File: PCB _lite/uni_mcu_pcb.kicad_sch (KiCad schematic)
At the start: 65 parts, among them J1 USB_C_Receptacle_USB2.0, J2 Conn_01x02_Male, J3 Conn_02x08_Odd_Even, Q1 Q_NPN_BCE, Q2 Q_NPN_BCE, Q3 Q_NPN_BCE, Q4 Q_NPN_BCE, Q5 FDS6890A, Q6 FDS6890A, SW1 SW_DIP_x01, SW2 SW_DIP_x01, SW3 SW_DIP_x01, U1 CC56-12CGKWA, U2 CH330N, U3 USBLC6-2P6, U4 STM32F030K6Tx, U5 LD1117S33TR_SOT223, U6 STM32F030C8Tx, U7 W25Q32JVSS, Y1 Crystal

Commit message: Добавлена lite версия платы
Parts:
- removed RN2: R_Pack05, Resistor_SMD:R_Array_Convex_5x0603, symbol Device:R_Pack05
- removed SW3: SW_DIP_x01, Button_Switch_SMD:SW_Push_1P1T_NO_Vertical_Wuerth_434133025816, symbol Switch:SW_DIP_x01
- removed U6: STM32F030C8Tx, Package_QFP:LQFP-48_7x7mm_P0.5mm, symbol MCU_ST_STM32F0:STM32F030C8Tx
- added J4: Conn_01x05_Female, TerminalBlock_MetzConnect:TerminalBlock_MetzConnect_Type011_RT05505HBWC_1x05_P5.00mm_Horizontal, symbol Connector:Conn_01x05_Female
- added R27, R28: R, Resistor_SMD:R_0603_1608Metric_Pad0.98x0.95mm_HandSolder, symbol Device:R
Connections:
- net I2C1_SDA is gone; now on net d_I2C1_SCL: R26.1
- net OUT3_CTRL is gone; now on net CA3_CTRL: R20.1, R24.2
- net OUT4_CTRL is gone; now on net CA4_CTRL: R18.1, R22.2
- net d is gone; now on net d_I2C1_SCL: U1.2 (d), U4.19 (PA9)
- net e is gone; now on net e_I2C1_SDA: U1.1 (e), U4.20 (PA10)
- net +3V3: no longer R25.2, R26.2
- net OUT1: now also J4.2 (Pin_2)
- net OUT2: now also J4.3 (Pin_3)
- net OUT3: now also J3.10 (Pin_10), J4.4 (Pin_4)
- net OUT4: now also J3.8 (Pin_8), J4.5 (Pin_5)
- net USART1_RX: no longer JP2.1 (A)
- net USART1_TX: no longer JP1.1 (A)
- net VCC: now also J4.1 (Pin_1)
- net a: now also JP1.1 (A)
- net b: now also JP2.1 (A)
- net c: now also R28.1
- net at J3.2 (Pin_2): now also R26.2
- net at J3.4 (Pin_4): now also R27.2
- net at J3.6 (Pin_6): now also R28.2
- net I2C1_SCL renamed d_I2C1_SCL
- net SW2 renamed e_I2C1_SDA
- net e_I2C1_SDA: now also R27.1
- no-connect marks 4 -> 1
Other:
- moved on the sheet: C6, C7, J3, R13, RN1, SW1, U4, Y1

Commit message: Частично разведена плата
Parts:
- removed RN1: R_Pack05, Resistor_SMD:R_Array_Convex_5x0603, symbol Device:R_Pack05
- removed U3: USBLC6-2P6, Package_TO_SOT_SMD:SOT-666, symbol Power_Protection:USBLC6-2P6
- removed U7: W25Q32JVSS, Package_SO:SOIC-8_5.23x5.23mm_P1.27mm, symbol Memory_Flash:W25Q32JVSS
- added J5: Conn_01x04_Female, Connector_Hirose:Hirose_DF11-4DP-2DSA_2x02_P2.00mm_Vertical, symbol Connector:Conn_01x04_Female
- added R29, R30, R31, R32: R, Resistor_SMD:R_0603_1608Metric_Pad0.98x0.95mm_HandSolder, symbol Device:R
- J2: footprint Connector_PinHeader_2.54mm:PinHeader_1x02_P2.54mm_Vertical -> TerminalBlock_MetzConnect:TerminalBlock_MetzConnect_Type011_RT05502HBWC_1x02_P5.00mm_Horizontal
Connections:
- net +3V3: now also J5.4 (Pin_4); no longer R15.1
- net GND: now also J5.1 (Pin_1)
- net PB0_IO: now also R15.2
- net PB1_IO: now also R29.2
- net SPI1_MISO: now also R31.2
- net SPI1_MOSI: now also R32.2
- net SPI1_SCK: now also R30.2
- net b: now also U4.22 (PA12); no longer JP2.1 (A), U4.13 (PA7)
- net c: now also JP2.1 (A), U4.13 (PA7); no longer U4.18 (PA8)
- net d_I2C1_SCL: no longer U1.2 (d), U4.19 (PA9)
- net dpx_swdio: now also J5.2 (Pin_2)
- net e_I2C1_SDA: no longer U1.1 (e), U4.20 (PA10)
- net g: now also U4.12 (PA6); no longer U4.22 (PA12)
- net swclk: now also J5.3 (Pin_3)
- net at J3.9 (Pin_9): now also R32.1
- net at J3.7 (Pin_7): now also R31.1
- net at J3.5 (Pin_5): now also R30.1
- net at J3.3 (Pin_3): now also R29.1
- net at J3.1 (Pin_1): now also R15.1
- removed net a: JP1.1 (A), U1.11 (a), U4.12 (PA6)
- new net a_I2C1_SDA: U1.11 (a), U4.20 (PA10)
- new net d: JP1.1 (A), U1.2 (d), U4.18 (PA8)
- new net e_I2C1_SCL: U1.1 (e), U4.19 (PA9)
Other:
- moved on the sheet: JP1

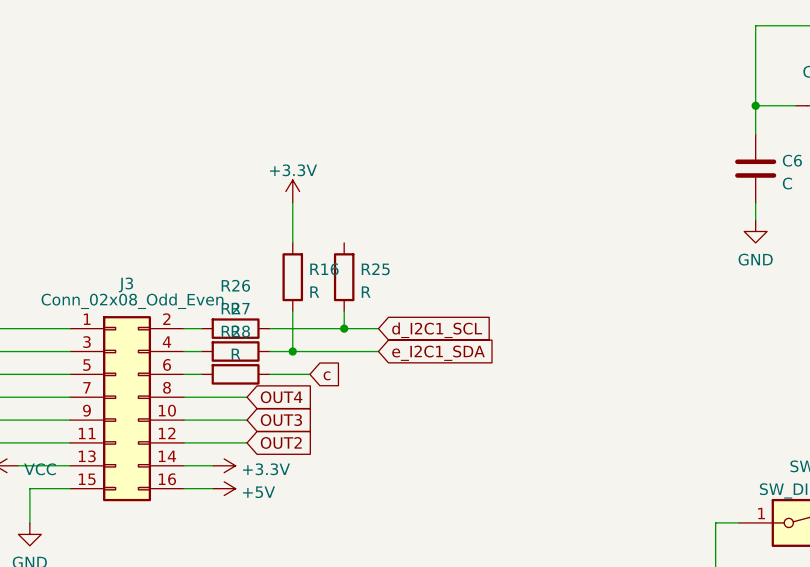
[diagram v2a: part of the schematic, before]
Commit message: разведена плата
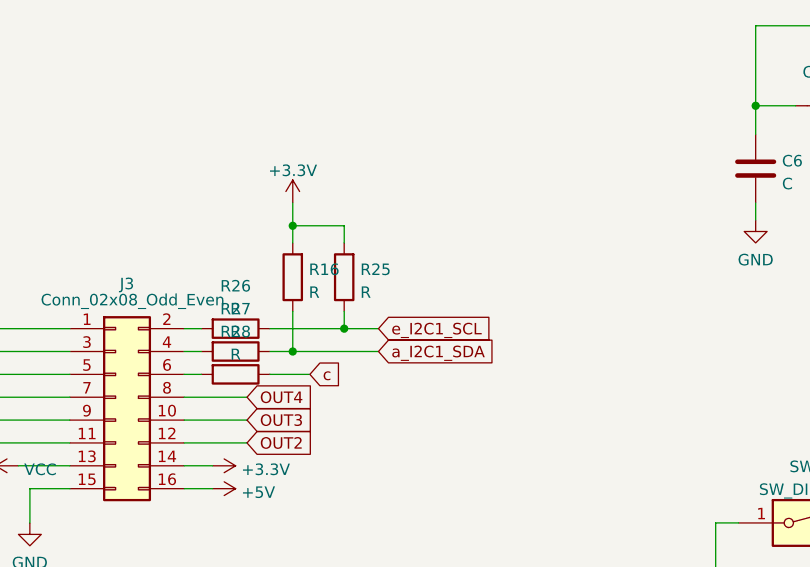
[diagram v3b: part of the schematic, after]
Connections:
- net d_I2C1_SCL is gone; now on net e_I2C1_SCL: R25.1, R26.1
- net e_I2C1_SDA is gone; now on net a_I2C1_SDA: R16.1, R27.1
- net +3V3: now also R25.2
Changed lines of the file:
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@@
   (junction (at 52.705 98.425) (diameter 0) (color 0 0 0 0)
+  )
+  (junction (at 191.77 142.24) (diameter 0) (color 0 0 0 0)
   )
   (junction (at 193.04 98.425) (diameter 0) (color 0 0 0 0)
@@
     (stroke (width 0) (type default) (color 0 0 0 0))
   )
+  (wire (pts (xy 191.77 142.24) (xy 191.77 144.145))
+    (stroke (width 0) (type default) (color 0 0 0 0))
+  )
   (wire (pts (xy 32.385 64.77) (xy 32.385 66.675))
     (stroke (width 0) (type default) (color 0 0 0 0))
@@
     (stroke (width 0) (type default) (color 0 0 0 0))
   )
+  (wire (pts (xy 197.485 144.145) (xy 197.485 142.24))
+    (stroke (width 0) (type default) (color 0 0 0 0))
+  )
   (wire (pts (xy 340.995 139.065) (xy 342.9 139.065))
     (stroke (width 0) (type default) (color 0 0 0 0))
@@
     (stroke (width 0) (type default) (color 0 0 0 0))
   )
-  (wire (pts (xy 191.77 139.7) (xy 191.77 144.145))
+  (wire (pts (xy 191.77 139.7) (xy 191.77 142.24))
     (stroke (width 0) (type default) (color 0 0 0 0))
   )
@@
   )
   (wire (pts (xy 36.195 121.285) (xy 36.195 118.745))
+    (stroke (width 0) (type default) (color 0 0 0 0))
+  )
+  (wire (pts (xy 197.485 142.24) (xy 191.77 142.24))
     (stroke (width 0) (type default) (color 0 0 0 0))
   )
@@
     )
   )
-  (global_label "d_I2C1_SCL" (shape input) (at 201.295 153.67 0) (fields_autoplaced)
-    (effects (font (size 1.27 1.27)) (justify left))
-    (property "Intersheet References" "${INTERSHEET_REFS}" (id 0) (at 214.5938 153.5906 0)
-      (effects (font (size 1.27 1.27)) (justify left) hide)
-    )
-  )
   (global_label "CA3_CTRL" (shape input) (at 295.91 224.79 180) (fields_autoplaced)
     (effects (font (size 1.27 1.27)) (justify right))
@@
     )
   )
-  (global_label "e_I2C1_SDA" (shape input) (at 201.295 156.21 0) (fields_autoplaced)
-    (effects (font (size 1.27 1.27)) (justify left))
-    (property "Intersheet References" "${INTERSHEET_REFS}" (id 0) (at 214.5938 156.1306 0)
+  (global_label "a_I2C1_SDA" (shape input) (at 201.295 156.21 0) (fields_autoplaced)
+    (effects (font (size 1.27 1.27)) (justify left))
+    (property "Intersheet References" "${INTERSHEET_REFS}" (id 0) (at 214.6543 156.1306 0)
       (effects (font (size 1.27 1.27)) (justify left) hide)
     )
@@
     (property "Intersheet References" "${INTERSHEET_REFS}" (id 0) (at 135.7145 156.1306 0)
       (effects (font (size 1.27 1.27)) (justify right) hide)
+    )
+  )
+  (global_label "e_I2C1_SCL" (shape input) (at 201.295 153.67 0) (fields_autoplaced)
+    (effects (font (size 1.27 1.27)) (justify left))
+    (property "Intersheet References" "${INTERSHEET_REFS}" (id 0) (at 214.5333 153.5906 0)
+      (effects (font (size 1.27 1.27)) (justify left) hide)
     )
   )
@@
     (pin "7")
     (pin "8")
+    (pin "3")
+    (pin "4")
+    (pin "5")
+    (pin "6")
   )
   (symbol (lib_id "power:GND") (at 112.395 45.085 0) (unit 1)
@@
       (effects (font (size 1.27 1.27)) (justify left) hide)
     )
+    (pin "1")
+    (pin "2")
+    (pin "7")
+    (pin "8")
     (pin "3")
     (pin "4")
@@
     (pin "7")
     (pin "8")
+    (pin "3")
+    (pin "4")
+    (pin "5")
+    (pin "6")
   )
   (symbol (lib_id "Simulation_SPICE:DIODE") (at 66.04 147.955 0) (unit 1)
@@
       (effects (font (size 1.27 1.27)) (justify left) hide)
     )
+    (pin "1")
+    (pin "2")
+    (pin "7")
+    (pin "8")
     (pin "3")
     (pin "4")

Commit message: Расставлены номиналы
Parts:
- C1, C10, C2, C3, C4, C5, C8: value C -> 0.1
- C6, C7: value C -> 22pF
- C9: value C -> 0.3
- D2: value DIODE -> SS24
- D3: value DIODE -> ss24
- D4: value D_TVS -> TVS24
- Q5, Q6: value FDS6890A -> F7313
- R1, R12, R13, R14, R2, R21, R22, R23, R24, R3, R4: value R -> 10K
- R10, R7, R8: value R -> 330
- R11, R15, R26, R27, R28, R29, R30, R31, R32, R9: value R -> 100
- R16, R25: value R -> 5.1K
- R17, R18, R19, R20, R5, R6: value R -> 1K
- Y1: value Crystal -> 8 Mhz
